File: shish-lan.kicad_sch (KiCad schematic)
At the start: 4 parts

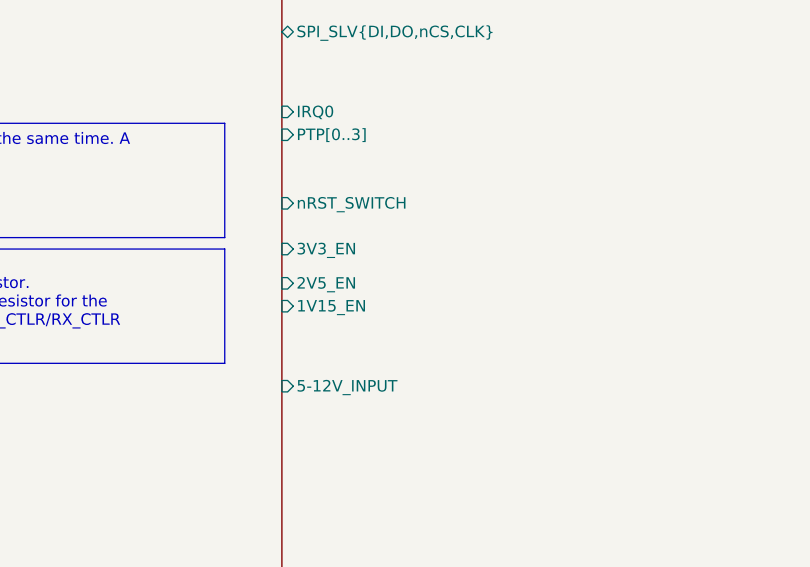
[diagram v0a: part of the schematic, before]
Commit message: renames 2V5 related nets
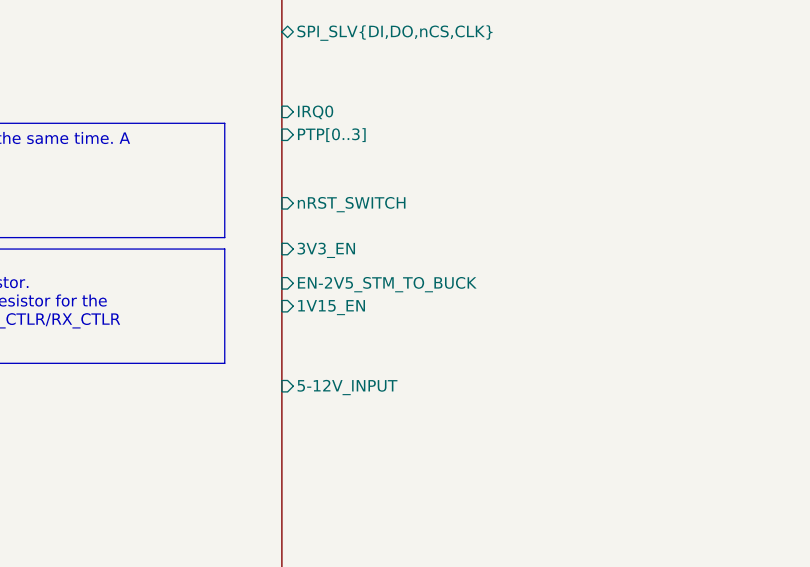
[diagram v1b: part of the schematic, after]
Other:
- sheet switch ports: added EN-2V5_STM_TO_BUCK; removed 2V5_EN
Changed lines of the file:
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@@
 			)
 		)
-		(pin "2V5_EN" input
+		(pin "EN-2V5_STM_TO_BUCK" input
 			(at 182.88 101.6 180)
 			(effects

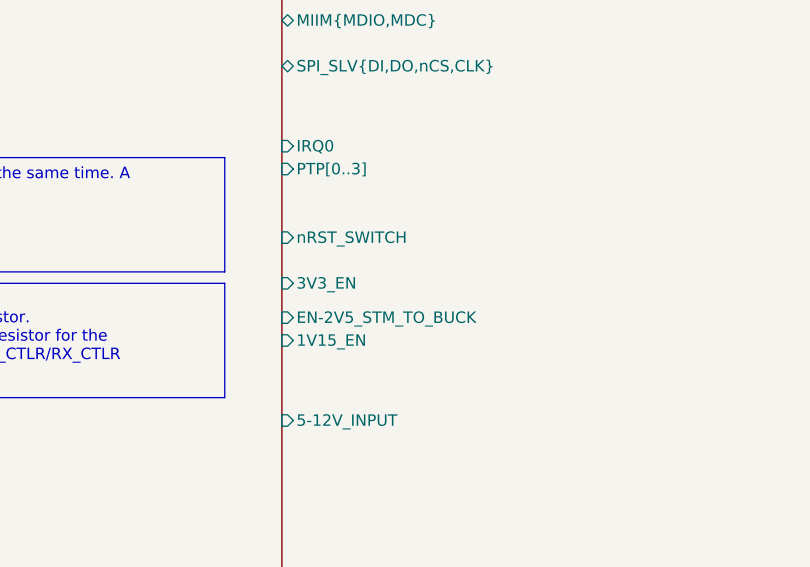
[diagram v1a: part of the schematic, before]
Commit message: renames 3V3 related nets
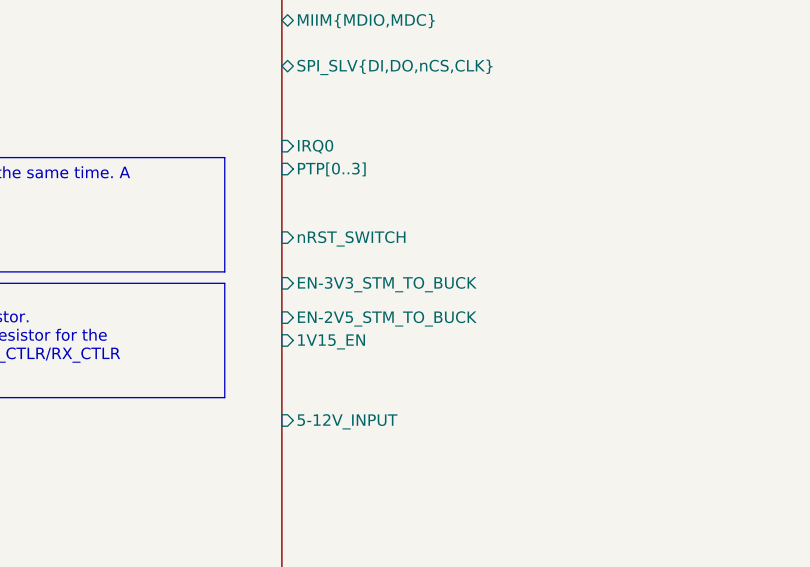
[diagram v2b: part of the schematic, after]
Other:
- sheet switch ports: added EN-3V3_STM_TO_BUCK; removed 3V3_EN
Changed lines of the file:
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@@
 			)
 		)
-		(pin "3V3_EN" input
+		(pin "EN-3V3_STM_TO_BUCK" input
 			(at 182.88 97.79 180)
 			(effects

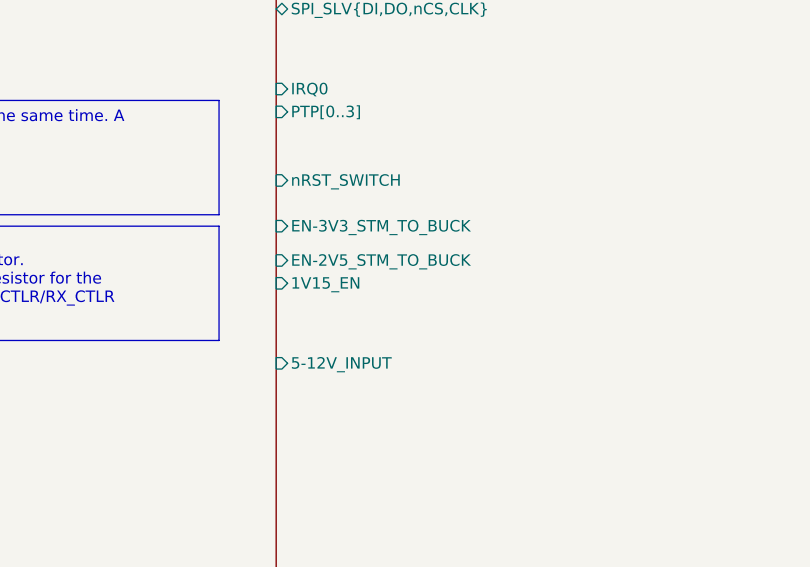
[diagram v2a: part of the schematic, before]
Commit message: renames 3V15 related nets
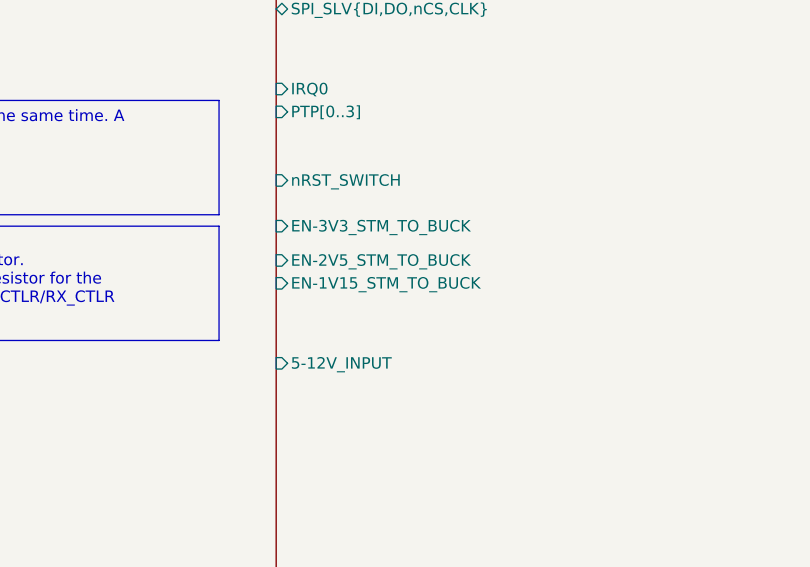
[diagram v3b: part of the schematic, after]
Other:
- sheet switch ports: added EN-1V15_STM_TO_BUCK; removed 1V15_EN
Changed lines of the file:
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@@
 			)
 		)
-		(pin "1V15_EN" input
+		(pin "EN-1V15_STM_TO_BUCK" input
 			(at 182.88 104.14 180)
 			(effects

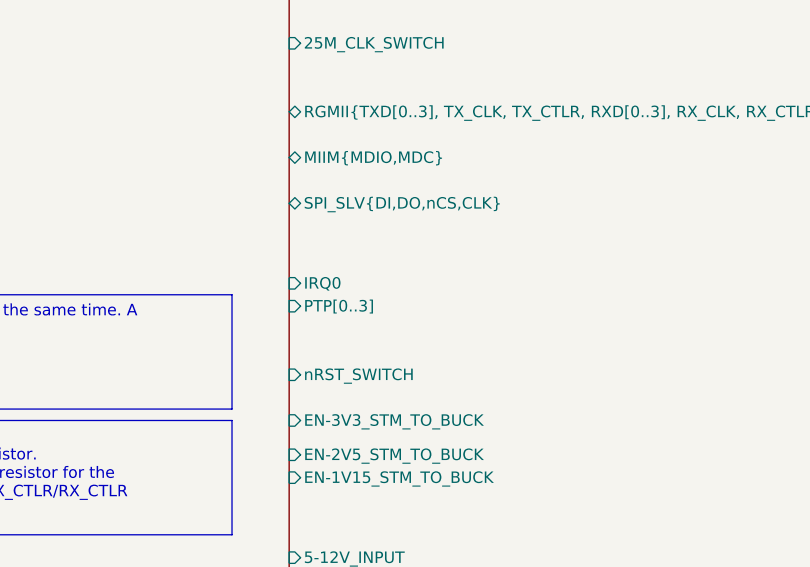
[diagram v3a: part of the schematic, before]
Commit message: updates IRQ0 related nets
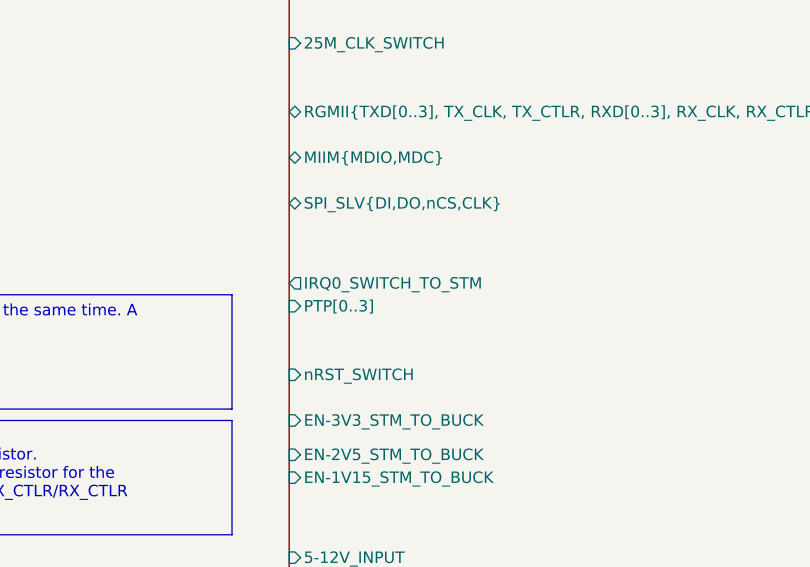
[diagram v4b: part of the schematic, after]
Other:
- sheet switch ports: added IRQ0_SWITCH_TO_STM; removed IRQ0
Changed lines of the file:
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@@
 			)
 		)
-		(pin "IRQ0" input
+		(pin "IRQ0_SWITCH_TO_STM" output
 			(at 182.88 82.55 180)
 			(effects

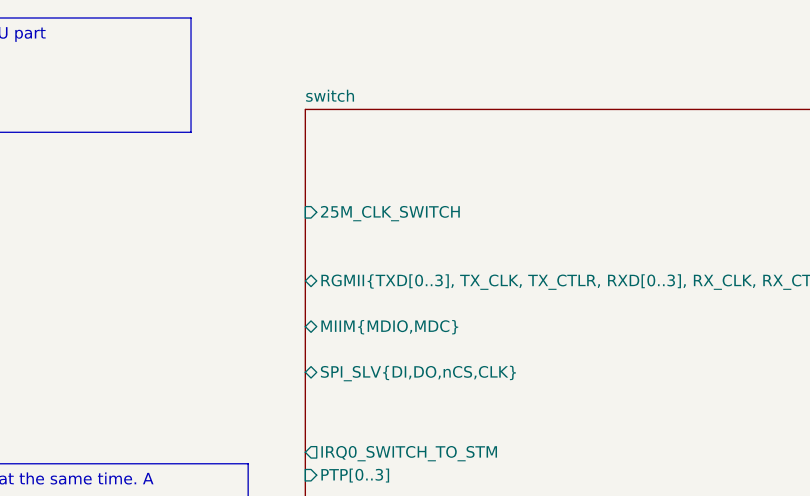
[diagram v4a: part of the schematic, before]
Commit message: updates 25MHz clock
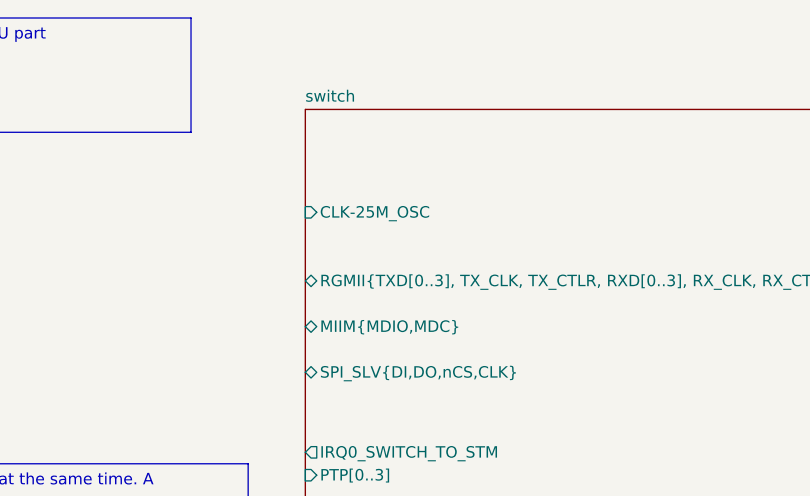
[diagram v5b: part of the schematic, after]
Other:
- sheet switch ports: added CLK-25M_OSC; removed 25M_CLK_SWITCH
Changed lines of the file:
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@@
 			)
 		)
-		(pin "25M_CLK_SWITCH" input
+		(pin "CLK-25M_OSC" input
 			(at 182.88 55.88 180)
 			(effects

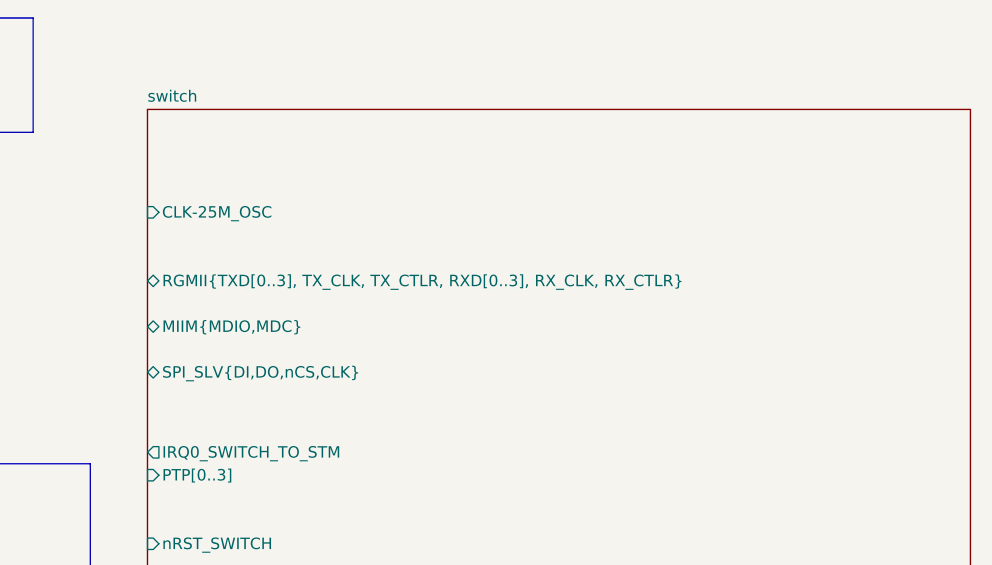
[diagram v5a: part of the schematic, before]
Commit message: updates RGMII bus to STM
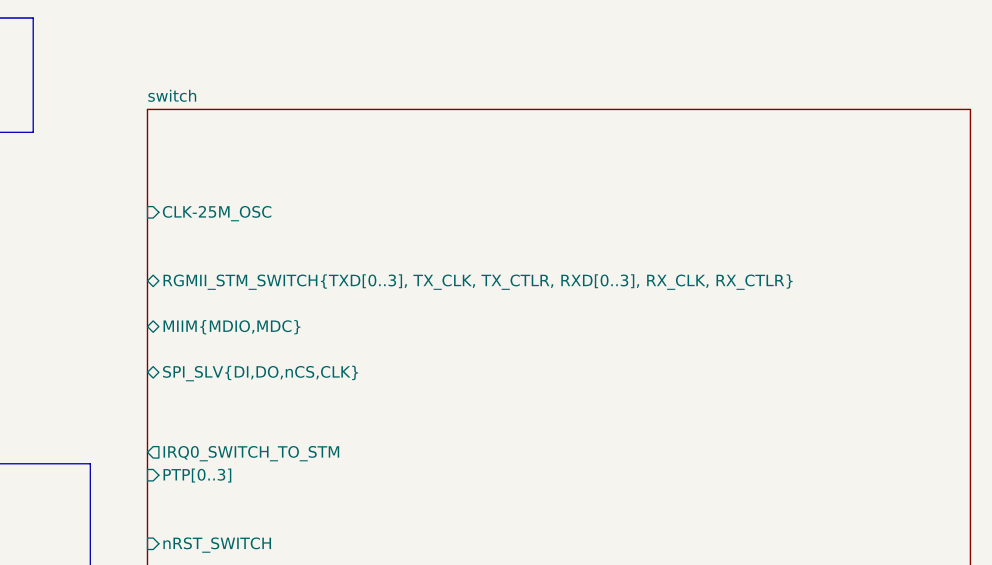
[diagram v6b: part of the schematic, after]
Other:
- sheet switch ports: added RGMII_STM_SWITCH{TXD[0..3], TX_CLK, TX_CTLR, RXD[0..3], RX_CLK, RX_CTLR}; removed RGMII{TXD[0..3], TX_CLK, TX_CTLR, RXD[0..3], RX_CLK, RX_CTLR}
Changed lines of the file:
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@@
 			)
 		)
-		(pin "RGMII{TXD[0..3], TX_CLK, TX_CTLR, RXD[0..3], RX_CLK, RX_CTLR}" bidirectional
-			(at 182.88 63.5 180)
+		(pin "RGMII_STM_SWITCH{TXD[0..3], TX_CLK, TX_CTLR, RXD[0..3], RX_CLK, RX_CTLR}"
+			bidirectional
+			(at 182.88 63.5 180
+			)
 			(effects
 				(font

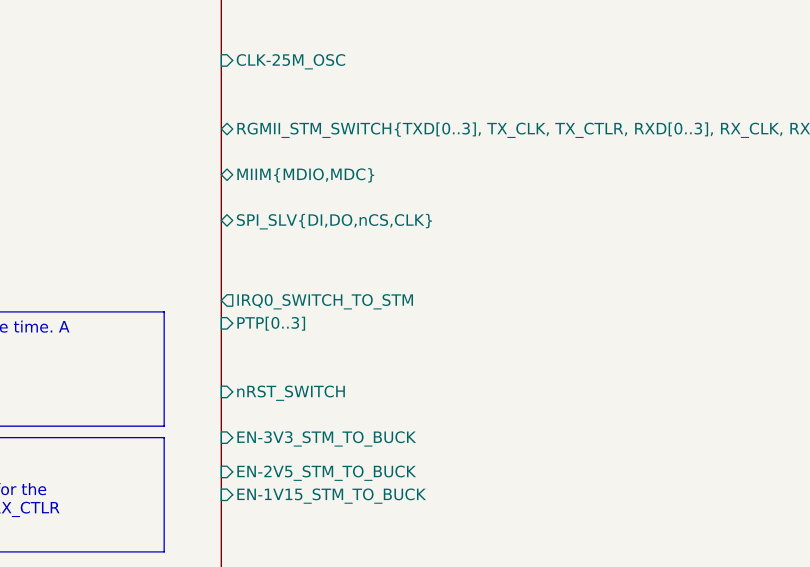
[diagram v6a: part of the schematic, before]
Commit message: updates MIIM bus to STM
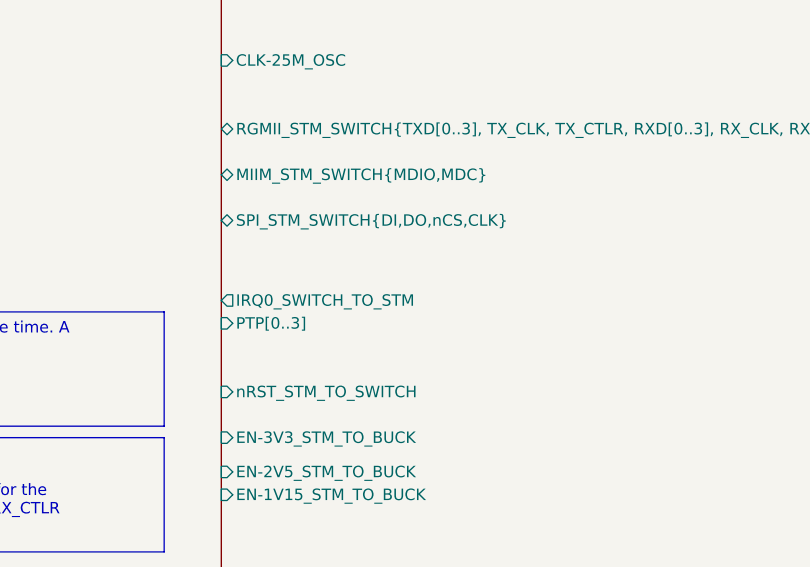
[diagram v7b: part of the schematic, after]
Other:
- sheet switch ports: added MIIM_STM_SWITCH{MDIO,MDC}, SPI_STM_SWITCH{DI,DO,nCS,CLK}, nRST_STM_TO_SWITCH; removed MIIM{MDIO,MDC}, SPI_SLV{DI,DO,nCS,CLK}, nRST_SWITCH
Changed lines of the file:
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@@
 			)
 		)
-		(pin "MIIM{MDIO,MDC}" bidirectional
+		(pin "MIIM_STM_SWITCH{MDIO,MDC}" bidirectional
 			(at 182.88 68.58 180)
 			(effects
@@
 			)
 		)
-		(pin "nRST_SWITCH" input
+		(pin "nRST_STM_TO_SWITCH" input
 			(at 182.88 92.71 180)
 			(effects
@@
 			)
 		)
-		(pin "SPI_SLV{DI,DO,nCS,CLK}" bidirectional
+		(pin "SPI_STM_SWITCH{DI,DO,nCS,CLK}" bidirectional
 			(at 182.88 73.66 180)
 			(effects
